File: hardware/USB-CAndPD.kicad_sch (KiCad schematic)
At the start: 33 parts, among them J201 USB_C_Receptacle_USB2.0_16P, J202 USB_C_Receptacle_USB2.0_16P, U201 TPS25730D, U202 TPD2E2U06DCK

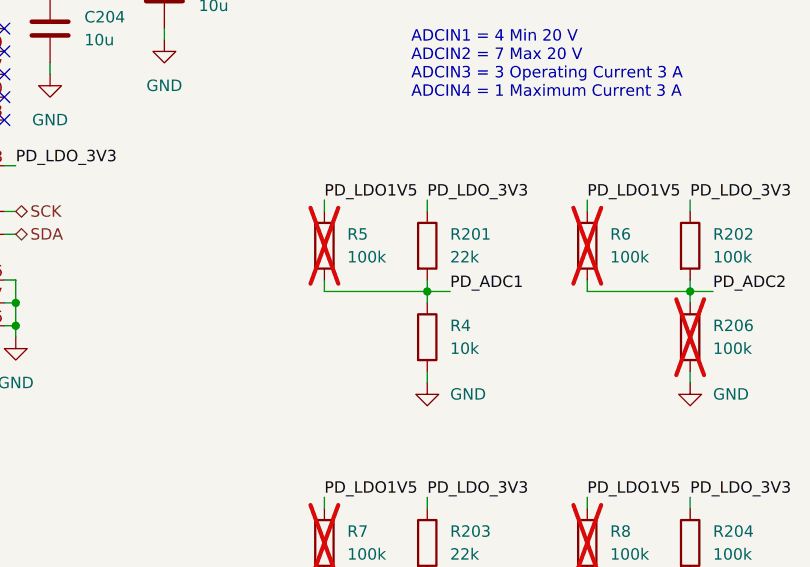
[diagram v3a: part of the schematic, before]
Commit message: Colored nets and added optional current measurement
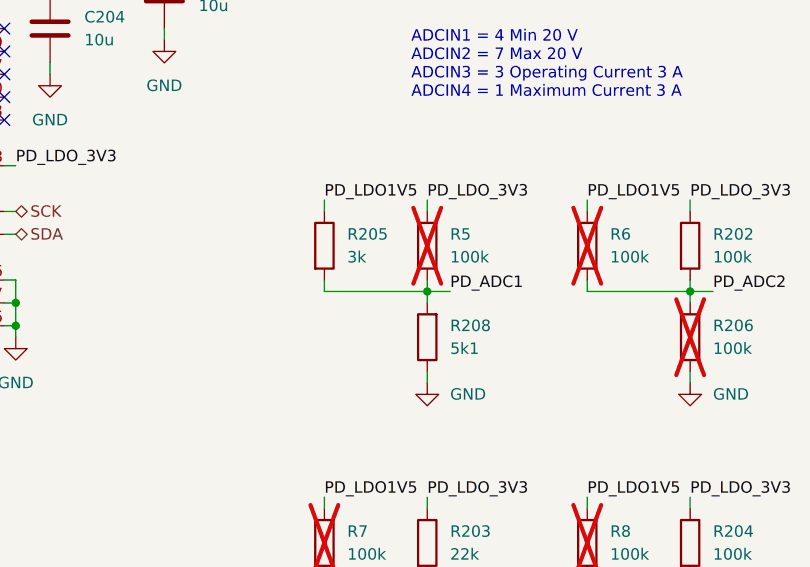
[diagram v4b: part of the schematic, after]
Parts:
- removed R201: 22k, Resistor_SMD:R_0603_1608Metric, symbol Device:R
- removed R4: 10k, Resistor_SMD:R_0603_1608Metric, symbol Device:R
- added R205: 3k, Resistor_SMD:R_0603_1608Metric, symbol Device:R
- added R208: 5k1, Resistor_SMD:R_0603_1608Metric, symbol Device:R
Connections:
- net GND: now also R208.1
- net PD_ADC1: now also R205.2, R208.2
- net PD_LDO1V5: now also R205.1; no longer R5.1
- net PD_LDO_3V3: now also R5.1
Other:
- moved on the sheet: R5
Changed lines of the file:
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@@
 	)
 	(symbol
-		(lib_id "Device:R")
-		(at 214.63 76.2 0)
-		(unit 1)
-		(exclude_from_sim no)
-		(in_bom yes)
-		(on_board yes)
-		(dnp no)
-		(fields_autoplaced yes)
-		(property "Reference" "R201"
-			(at 217.17 74.9299 0)
-			(effects
-				(font
-					(size 1.27 1.27)
-				)
-				(justify left)
-			)
-		)
-		(property "Value" "22k"
-			(at 217.17 77.4699 0)
-			(effects
-				(font
-					(size 1.27 1.27)
-				)
-				(justify left)
-			)
-		)
-		(property "Footprint" "Resistor_SMD:R_0603_1608Metric"
-			(at 212.852 76.2 90)
-			(effects
-				(font
-					(size 1.27 1.27)
-				)
-				(hide yes)
-			)
-		)
-		(property "Datasheet" "~"
-			(at 214.63 76.2 0)
-			(effects
-				(font
-					(size 1.27 1.27)
-				)
-				(hide yes)
-			)
-		)
-		(property "Description" "Resistor"
-			(at 214.63 76.2 0)
-			(effects
-				(font
-					(size 1.27 1.27)
-				)
-				(hide yes)
-			)
-		)
-		(property "Sim.Device" ""
-			(at 214.63 76.2 0)
-			(effects
-				(font
-					(size 1.27 1.27)
-				)
-			)
-		)
-		(property "Sim.Type" ""
-			(at 214.63 76.2 0)
-			(effects
-				(font
-					(size 1.27 1.27)
-				)
-			)
-		)
-		(property "OrderLink" ""
-			(at 214.63 76.2 0)
-			(effects
-				(font
-					(size 1.27 1.27)
-				)
-			)
-		)
-		(property "Qty" ""
-			(at 214.63 76.2 0)
-			(effects
-				(font
-					(size 1.27 1.27)
-				)
-			)
-		)
-		(pin "2"
-		)
-		(pin "1"
-		)
-		(instances
-			(project "glowbuck"
-				(path "/5c22e6dd-0c33-4422-b6db-bb3ef40a8534/e97aabf0-d438-4347-9d51-84dd12990013"
-					(reference "R201")
-					(unit 1)
-				)
-			)
-		)
-	)
-	(symbol
 		(lib_id "power:GND")
 		(at 127 44.45 0)
@@
 	(symbol
 		(lib_id "Device:R")
-		(at 214.63 86.36 0)
+		(at 203.2 76.2 0)
 		(unit 1)
 		(exclude_from_sim no)
@@
 		(dnp no)
 		(fields_autoplaced yes)
-		(property "Reference" "R4"
-			(at 217.17 85.0899 0)
+		(property "Reference" "R205"
+			(at 205.74 74.9299 0)
 			(effects
 				(font
@@
 			)
 		)
-		(property "Value" "10k"
-			(at 217.17 87.6299 0)
+		(property "Value" "3k"
+			(at 205.74 77.4699 0)
 			(effects
 				(font
@@
 		)
 		(property "Footprint" "Resistor_SMD:R_0603_1608Metric"
-			(at 212.852 86.36 90)
+			(at 201.422 76.2 90)
 			(effects
 				(font
@@
 		)
 		(property "Datasheet" "~"
-			(at 214.63 86.36 0)
+			(at 203.2 76.2 0)
 			(effects
 				(font
@@
 		)
 		(property "Description" "Resistor"
-			(at 214.63 86.36 0)
-			(effects
-				(font
-					(size 1.27 1.27)
-				)
-				(hide yes)
-			)
-		)
-		(property "Sim.Device" ""
-			(at 214.63 86.36 0)
-			(effects
-				(font
-					(size 1.27 1.27)
-				)
-			)
-		)
-		(property "Sim.Type" ""
-			(at 214.63 86.36 0)
-			(effects
-				(font
-					(size 1.27 1.27)
-				)
-			)
-		)
-		(property "OrderLink" ""
-			(at 214.63 86.36 0)
-			(effects
-				(font
-					(size 1.27 1.27)
-				)
-			)
-		)
-		(property "MouserNumber" "603-RT0603FRE07100KL"
-			(at 214.63 86.36 0)
+			(at 203.2 76.2 0)
 			(effects
 				(font
@@
 			)
 		)
-		(property "Qty" ""
-			(at 214.63 86.36 0)
-			(effects
-				(font
-					(size 1.27 1.27)
-				)
-			)
+		(pin "1"
 		)
 		(pin "2"
 		)
-		(pin "1"
-		)
 		(instances
 			(project "glowbuck"
 				(path "/5c22e6dd-0c33-4422-b6db-bb3ef40a8534/e97aabf0-d438-4347-9d51-84dd12990013"
-					(reference "R4")
+					(reference "R205")
 					(unit 1)
 				)
@@
 	(symbol
 		(lib_id "Device:R")
-		(at 203.2 76.2 0)
+		(at 214.63 76.2 0)
 		(unit 1)
 		(exclude_from_sim no)
@@
 		(fields_autoplaced yes)
 		(property "Reference" "R5"
-			(at 205.74 74.9299 0)
+			(at 217.17 74.9299 0)
 			(effects
 				(font
@@
 		)
 		(property "Value" "100k"
-			(at 205.74 77.4699 0)
+			(at 217.17 77.4699 0)
 			(effects
 				(font
@@
 		)
 		(property "Footprint" "Resistor_SMD:R_0603_1608Metric"
-			(at 201.422 76.2 90)
+			(at 212.852 76.2 90)
 			(effects
 				(font
@@
 		)
 		(property "Datasheet" "~"
-			(at 203.2 76.2 0)
+			(at 214.63 76.2 0)
 			(effects
 				(font
@@
 		)
 		(property "Description" "Resistor"
-			(at 203.2 76.2 0)
+			(at 214.63 76.2 0)
 			(effects
 				(font
@@
 		)
 		(property "Sim.Device" ""
-			(at 203.2 76.2 0)
+			(at 214.63 76.2 0)
 			(effects
 				(font
@@
 		)
 		(property "Sim.Type" ""
-			(at 203.2 76.2 0)
+			(at 214.63 76.2 0)
 			(effects
 				(font
@@
 		)
 		(property "OrderLink" ""
-			(at 203.2 76.2 0)
+			(at 214.63 76.2 0)
 			(effects
 				(font
@@
 		)
 		(property "Qty" ""
-			(at 203.2 76.2 0)
+			(at 214.63 76.2 0)
 			(effects
 				(font
@@
 					(unit 1)
 				)
+			)
+		)
+	)
+	(symbol
+		(lib_id "Device:R")
+		(at 214.63 86.36 180)
+		(unit 1)
+		(exclude_from_sim no)
+		(in_bom yes)
+		(on_board yes)
+		(dnp no)
+		(fields_autoplaced yes)
+		(property "Reference" "R208"
+			(at 217.17 85.0899 0)
+			(effects
+				(font
+					(size 1.27 1.27)
+				)
+				(justify right)
+			)
+		)
+		(property "Value" "5k1"
+			(at 217.17 87.6299 0)
+			(effects
+				(font
+					(size 1.27 1.27)
+				)
+				(justify right)
+			)
+		)
+		(property "Footprint" "Resistor_SMD:R_0603_1608Metric"
+			(at 216.408 86.36 90)
+			(effects
+				(font
+					(size 1.27 1.27)
+				)
+				(hide yes)
+			)
+		)
+		(property "Datasheet" "~"
+			(at 214.63 86.36 0)
+			(effects
+				(font
+					(size 1.27 1.27)
+				)
+				(hide yes)
+			)
+		)
+		(property "Description" "Resistor"
+			(at 214.63 86.36 0)
+			(effects
+				(font
+					(size 1.27 1.27)
+				)
+				(hide yes)
+			)
+		)
+		(property "Sim.Device" ""
+			(at 214.63 86.36 0)
+			(effects
+				(font
+					(size 1.27 1.27)
+				)
+			)
+		)
+		(property "Sim.Type" ""
+			(at 214.63 86.36 0)
+			(effects
+				(font
+					(size 1.27 1.27)
+				)
+			)
+		)
+		(property "OrderLink" ""
+			(at 214.63 86.36 0)
+			(effects
+				(font
+					(size 1.27 1.27)
+				)
+			)
+		)
+		(property "MouserNumber" "603-RT0603DRE075K11L"
+			(at 214.63 86.36 0)
+			(effects
+				(font
+					(size 1.27 1.27)
+				)
+				(hide yes)
+			)
+		)
+		(property "Var" "Debug Included(5k1) Excluded(-! DNP)"
+			(at 214.63 86.36 0)
+			(effects
+				(font
+					(size 1.27 1.27)
+				)
+				(hide yes)
+			)
+		)
+		(property "Qty" ""
+			(at 214.63 86.36 0)
+			(effects
+				(font
+					(size 1.27 1.27)
+				)
+			)
+		)
+		(pin "2"
+		)
+		(pin "1"
+		)
+		(instances
+			(project "glowbuck"
+				(path "/5c22e6dd-0c33-4422-b6db-bb3ef40a8534/e97aabf0-d438-4347-9d51-84dd12990013"
+					(reference "R208")
+					(unit 1)
+				)

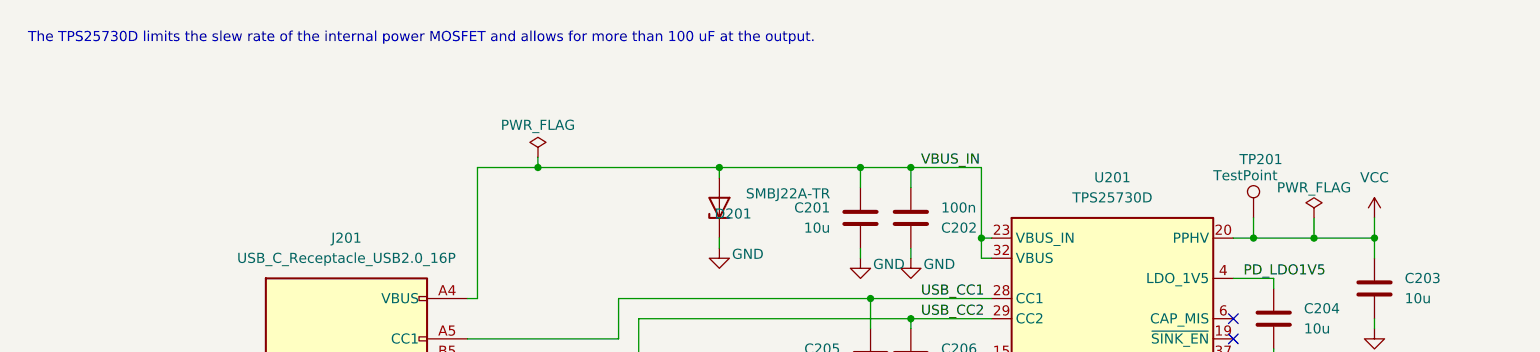
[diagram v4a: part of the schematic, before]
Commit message: Global labels, explanation texts, fix spring connector
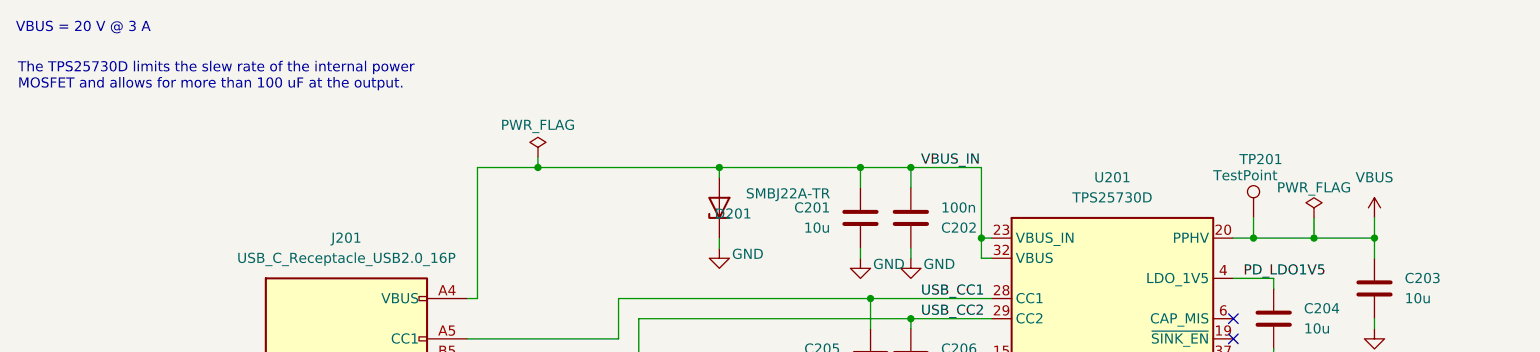
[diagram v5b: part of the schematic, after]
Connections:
- net VCC renamed VBUS
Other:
- note added: "VBUS = 20 V @ 3 A"
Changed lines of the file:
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@@
 		(title "Glowbuck")
 	)
-	(text "The TPS25730D limits the slew rate of the internal power MOSFET and allows for more than 100 uF at the output."
+	(text "The TPS25730D limits the slew rate of the internal power\nMOSFET and allows for more than 100 uF at the output."
 		(exclude_from_sim no)
-		(at 15.748 16.002 0)
+		(at 14.478 19.812 0)
 		(effects
 			(font
@@
 		)
 	)
+	(text "VBUS = 20 V @ 3 A"
+		(exclude_from_sim no)
+		(at 14.224 14.732 0)
+		(effects
+			(font
+				(size 1.27 1.27)
+			)
+			(justify left top)
+		)
+	)
 	(junction
 		(at 214.63 114.3)
@@
 	)
 	(symbol
-		(lib_id "power:VCC")
-		(at 185.42 39.37 0)
-		(unit 1)
-		(exclude_from_sim no)
-		(in_bom yes)
-		(on_board yes)
-		(dnp no)
-		(fields_autoplaced yes)
-		(property "Reference" "#PWR0201"
-			(at 185.42 43.18 0)
-			(effects
-				(font
-					(size 1.27 1.27)
-				)
-				(hide yes)
-			)
-		)
-		(property "Value" "VCC"
-			(at 185.42 34.29 0)
-			(effects
-				(font
-					(size 1.27 1.27)
-				)
-			)
-		)
-		(property "Footprint" ""
-			(at 185.42 39.37 0)
-			(effects
-				(font
-					(size 1.27 1.27)
-				)
-				(hide yes)
-			)
-		)
-		(property "Datasheet" ""
-			(at 185.42 39.37 0)
-			(effects
-				(font
-					(size 1.27 1.27)
-				)
-				(hide yes)
-			)
-		)
-		(property "Description" "Power symbol creates a global label with name \"VCC\""
-			(at 185.42 39.37 0)
-			(effects
-				(font
-					(size 1.27 1.27)
-				)
-				(hide yes)
-			)
-		)
-		(pin "1"
-		)
-		(instances
-			(project "glowbuck"
-				(path "/5c22e6dd-0c33-4422-b6db-bb3ef40a8534/e97aabf0-d438-4347-9d51-84dd12990013"
-					(reference "#PWR0201")
-					(unit 1)
-				)
-			)
-		)
-	)
-	(symbol
 		(lib_id "power:GND")
 		(at 172.72 57.15 0)
@@
 					(unit 1)
 				)
+			)
+		)
+	)
+	(symbol
+		(lib_id "power:VBUS")
+		(at 185.42 39.37 0)
+		(unit 1)
+		(exclude_from_sim no)
+		(in_bom yes)
+		(on_board yes)
+		(dnp no)
+		(fields_autoplaced yes)
+		(property "Reference" "#PWR0201"
+			(at 185.42 43.18 0)
+			(effects
+				(font
+					(size 1.27 1.27)
+				)
+				(hide yes)
+			)
+		)
+		(property "Value" "VBUS"
+			(at 185.42 34.29 0)
+			(effects
+				(font
+					(size 1.27 1.27)
+				)
+			)
+		)
+		(property "Footprint" ""
+			(at 185.42 39.37 0)
+			(effects
+				(font
+					(size 1.27 1.27)
+				)
+				(hide yes)
+			)
+		)
+		(property "Datasheet" ""
+			(at 185.42 39.37 0)
+			(effects
+				(font
+					(size 1.27 1.27)
+				)
+				(hide yes)
+			)
+		)
+		(property "Description" "Power symbol creates a global label with name \"VBUS\""
+			(at 185.42 39.37 0)
+			(effects
+				(font
+					(size 1.27 1.27)
+				)
+				(hide yes)
+			)
+		)
+		(pin "1"
+		)
+		(instances
+			(project "glowbuck"
+				(path "/5c22e6dd-0c33-4422-b6db-bb3ef40a8534/e97aabf0-d438-4347-9d51-84dd12990013"
+					(reference "#PWR0201")
+					(unit 1)
+				)

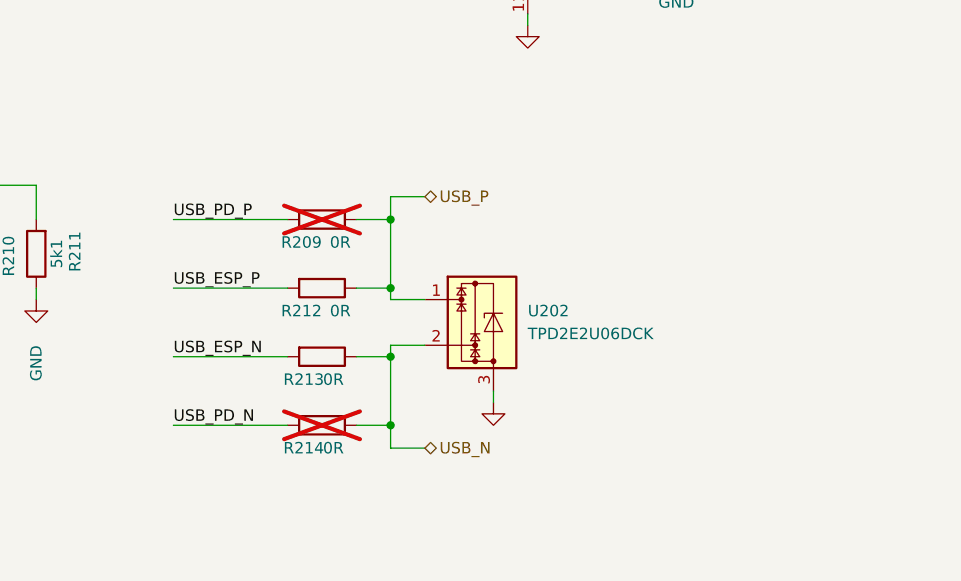
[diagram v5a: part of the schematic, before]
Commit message: Layout Stecker final, USB done, buck wip
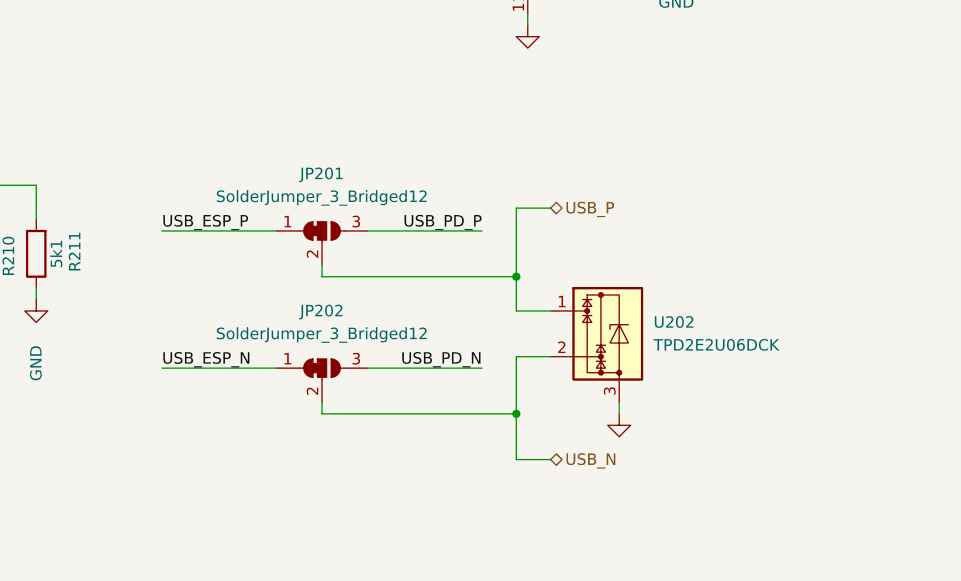
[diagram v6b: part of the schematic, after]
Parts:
- removed R209, R212, R213, R214: 0R, Resistor_SMD:R_0603_1608Metric, symbol Device:R
- added JP201, JP202: SolderJumper_3_Bridged12, glowbuck:SolderJumper_123_0603, symbol Jumper:SolderJumper_3_Bridged12
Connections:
- net USB_ESP_N: now also JP202.1 (A)
- net USB_ESP_P: now also JP201.1 (A)
- net USB_N: now also JP202.2 (C)
- net USB_P: now also JP201.2 (C)
- net USB_PD_N: now also JP202.3 (B)
- net USB_PD_P: now also JP201.3 (B)
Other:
- moved on the sheet: U202

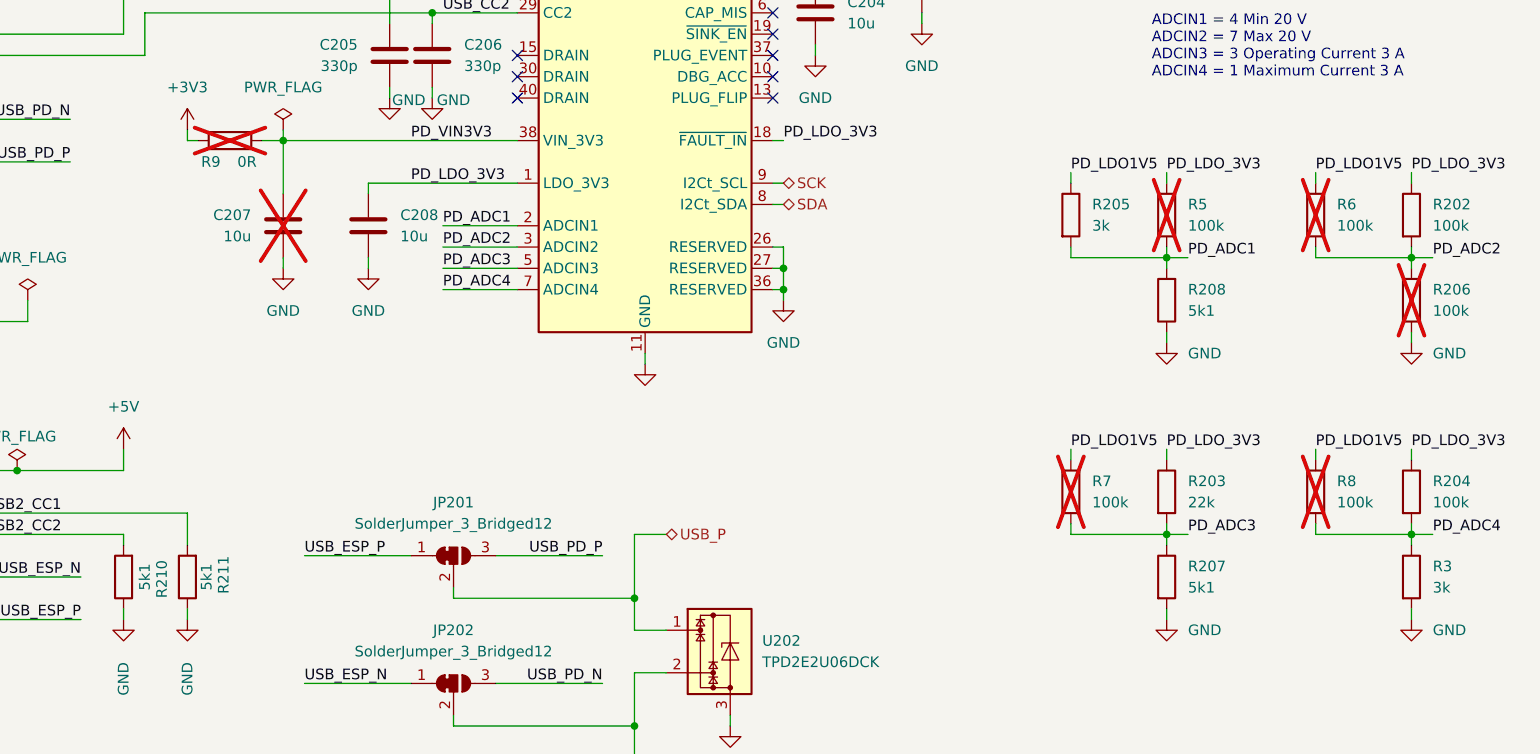
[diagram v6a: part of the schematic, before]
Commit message: Layout in progress. I2C done
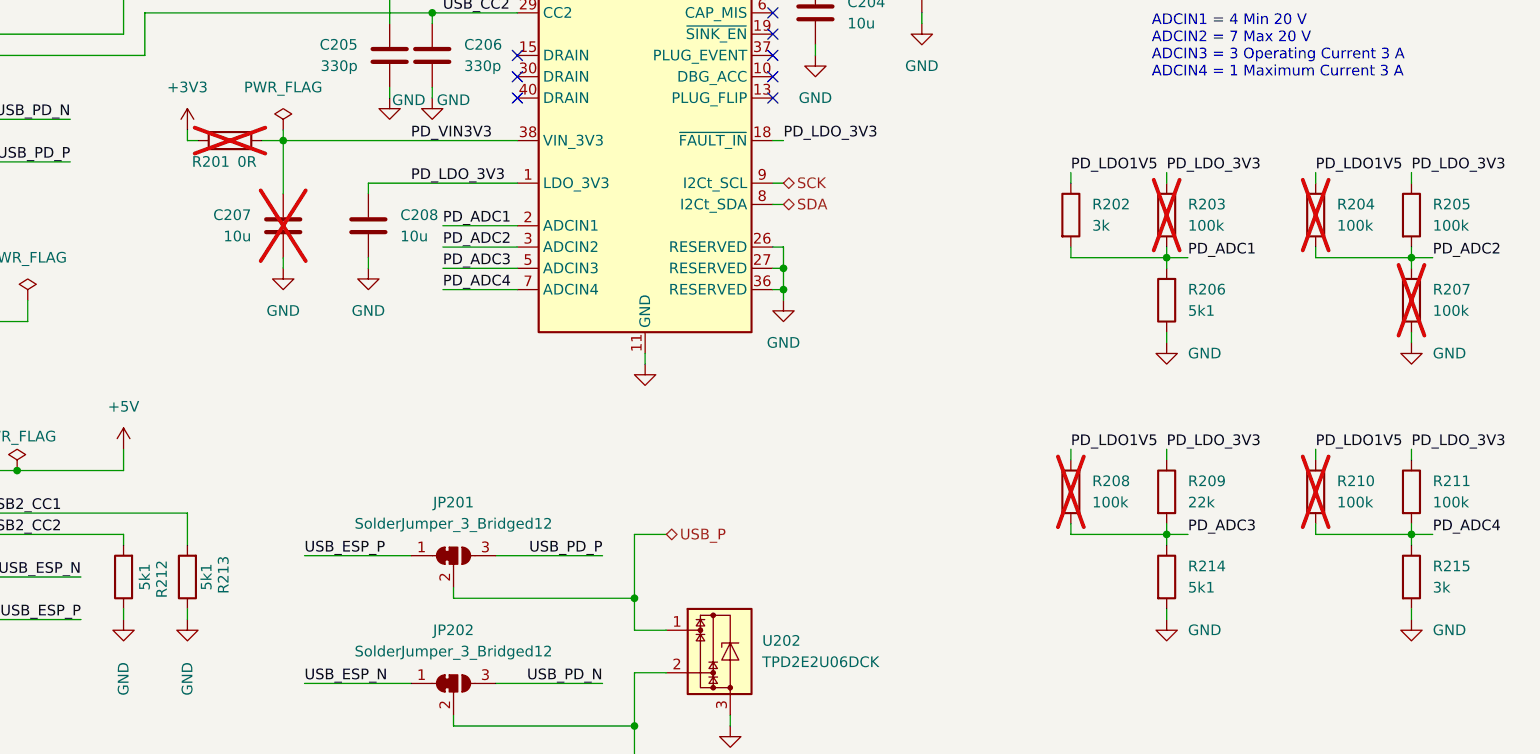
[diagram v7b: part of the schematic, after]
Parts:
- renumbered R9 to R201, R205 to R202, R5 to R203, R6 to R204, R202 to R205, R208 to R206, R206 to R207, R7 to R208, R203 to R209, R8 to R210, R204 to R211, R210 to R212, R211 to R213, R207 to R214, R3 to R215

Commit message: Added ManufacturerNumber for every item and fixed bom errors
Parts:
- C201, C203: ManufacturerNumber (none) -> CL32B106KBJNNNE
- C202: ManufacturerNumber (none) -> CL10B104KB8WPND
- C204, C207, C208: ManufacturerNumber (none) -> CL10A106MA8NRNC
- C205, C206: ManufacturerNumber (none) -> C0603C331K5RACTU
- D201: ManufacturerNumber (none) -> SMBJ22A-TR
- J201, J202: ManufacturerNumber (none) -> USB4105-GF-A
- R201: ManufacturerNumber (none) -> RC0603FR-130RL
- R202: ManufacturerNumber (none) -> RC0603FR-133KL; MouserNumber (none) -> 603-RC0603FR-133KL
- R203, R204, R207, R208, R210: ManufacturerNumber (none) -> RT0603FRE07100KL; MouserNumber (none) -> 603-RT0603FRE07100KL
- R205, R211: ManufacturerNumber (none) -> RT0603FRE07100KL
- R206, R212, R213, R214: ManufacturerNumber (none) -> RT0603DRE075K11L
- R209: ManufacturerNumber (none) -> RT0603DRE0722KL; MouserNumber 603-RT0603FRE07100KL -> 603-RT0603DRE0722KL
- R215: ManufacturerNumber (none) -> RC0603FR-133KL; MouserNumber 603-RT0603DRE075K11L -> 603-RC0603FR-133KL
- U201: ManufacturerNumber (none) -> TPS25730DREFR
- U202: ManufacturerNumber (none) -> TPD2E2U06QDCKRQ1
